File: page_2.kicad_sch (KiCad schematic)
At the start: 41 parts, among them J3 Conn_01x05, J601 USB_C_Receptacle_USB2.0_16P, SW1 SW_Push, SW2 SW_Push, T201 TP 201, U3 TCA9535PWR, U4 TCA9535PWR, U601 USBLC6-2SC6, U602 USBLC6-2SC6

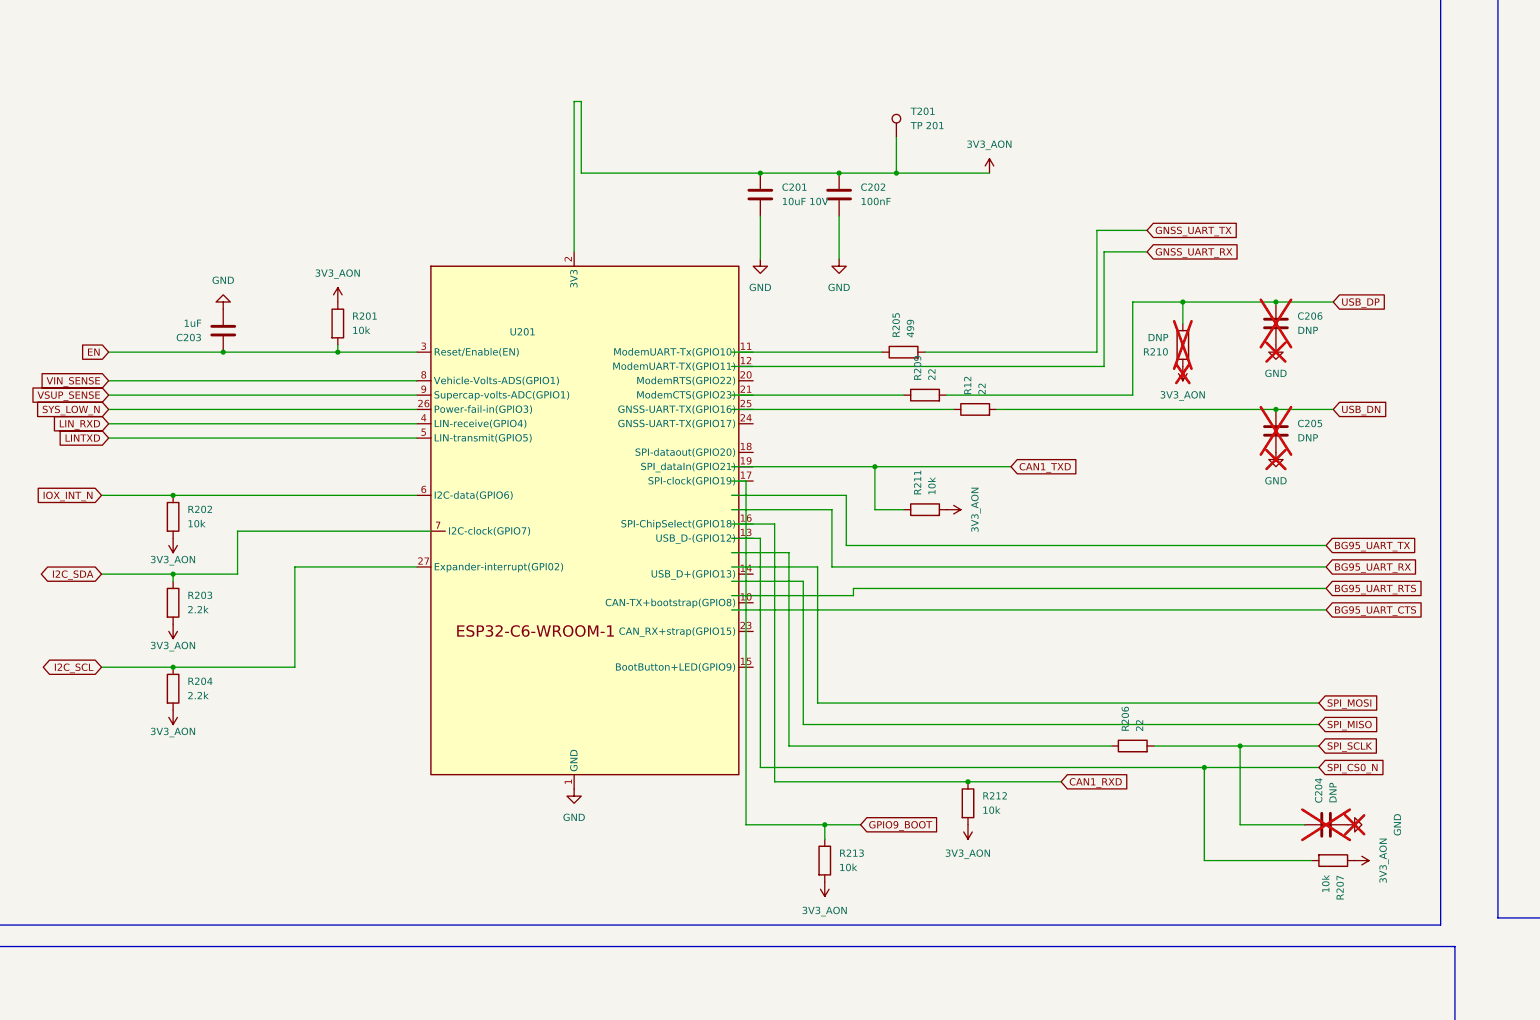
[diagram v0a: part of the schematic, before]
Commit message: Rework ESP32-C6 schematic routing
Updated the ESP32-C6-WROOM-1 schematic placement, pin naming, and net routing to match the intended board connectivity. This includes repositioning junctions/wires, correcting signal names like VehicleVolts-ADS and SupercapVolts-ADC, and aligning global labels/power symbols with the revised layout.
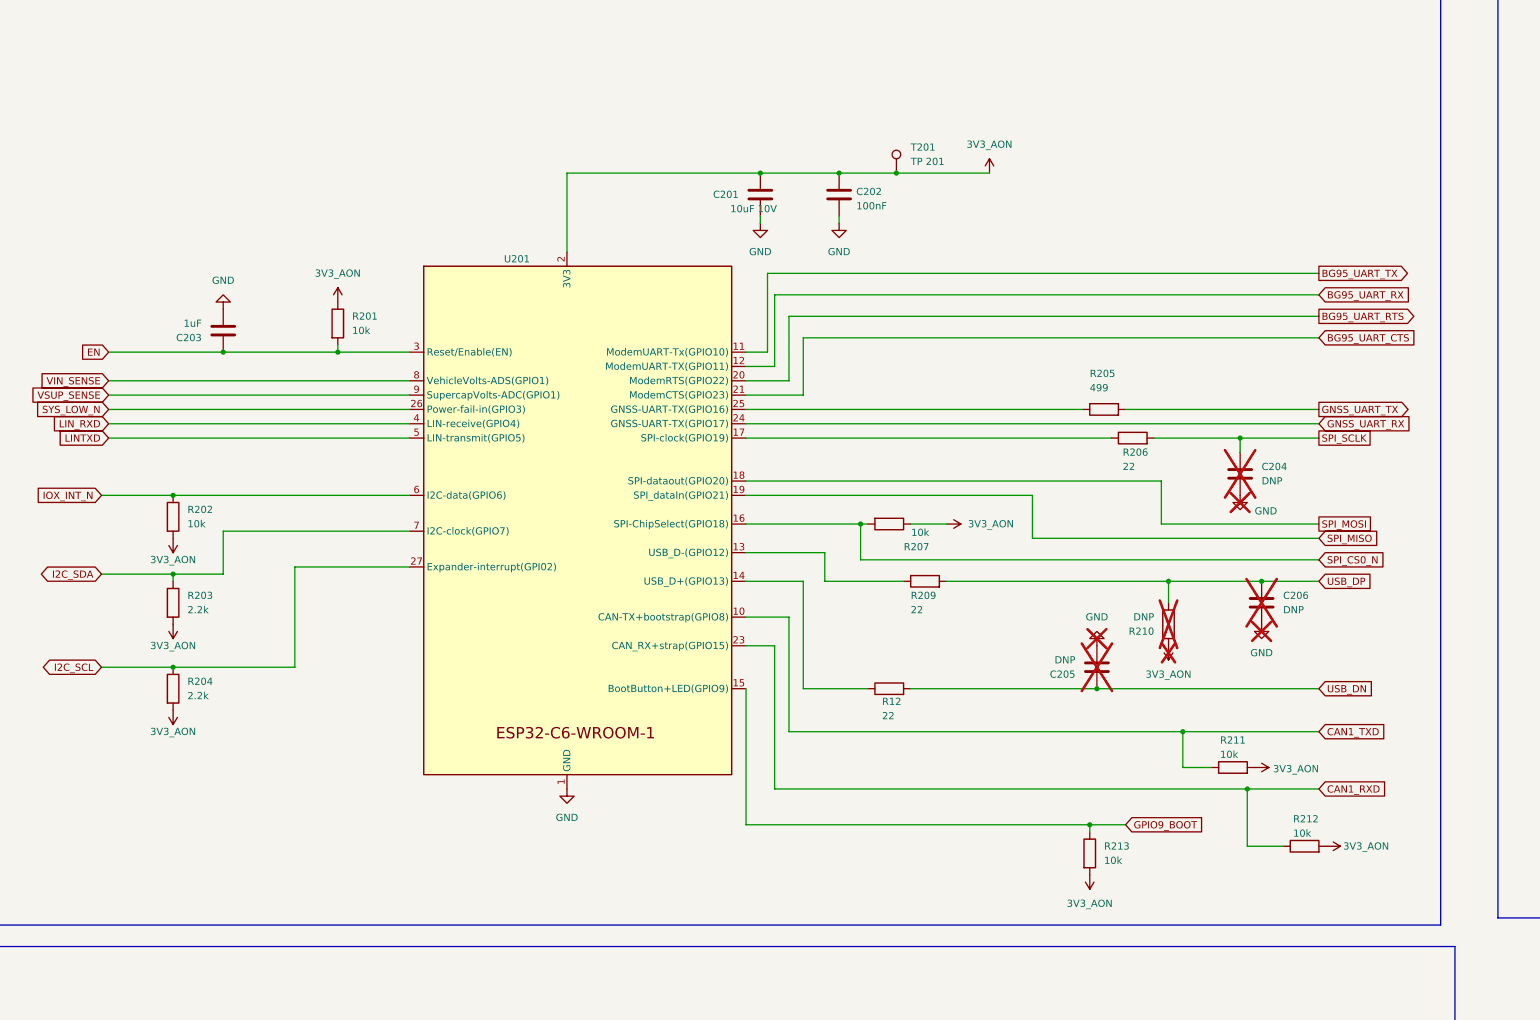
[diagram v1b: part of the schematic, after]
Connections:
- net BG95_UART_CTS: now also U201.21 (ModemCTS(GPIO23))
- net BG95_UART_RTS: now also U201.20 (ModemRTS(GPIO22))
- net BG95_UART_RX: now also U201.12 (ModemUART-TX(GPIO11))
- net BG95_UART_TX: now also U201.11 (ModemUART-Tx(GPIO10))
- net CAN1_RXD: now also U201.23 (CAN_RX+strap(GPIO15))
- net CAN1_TXD: now also U201.10 (CAN-TX+bootstrap(GPIO8))
- net GNSS_UART_RX: now also U201.24 (GNSS-UART-TX(GPIO17))
- net GPIO9_BOOT: now also U201.15 (BootButton+LED(GPIO9))
- net SPI_CS0_N: now also U201.16 (SPI-ChipSelect(GPIO18))
- net SPI_MISO: now also U201.19 (SPI_dataIn(GPIO21))
- net SPI_MOSI: now also U201.18 (SPI-dataout(GPIO20))
- net at R206.1: now also U201.17 (SPI-clock(GPIO19))
- net at R209.1: now also U201.13 (USB_D-(GPIO12))
- net at R12.1: now also U201.14 (USB_D+(GPIO13))
- net at R205.1: now also U201.25 (GNSS-UART-TX(GPIO16))
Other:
- moved on the sheet: C204, C205, C206, R12, R205, R206, R207, R209, R210, R211, R212, R213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

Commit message: Rework power/reset and USB protection
This schematic update adds a reset supervisor and associated support components, reworks the USB-C protection network and connector layout, and adds boot/reset/testpoint circuitry. It also reorganizes the ESP32-related blocks, updates labels and power nets, and moves the I/O-expander and peripheral sections to match the revised design.
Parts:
- removed C3: C, Package_SO:TSSOP-24_4.4x7.8mm_P0.65mm, symbol Device:C
- removed J3: Conn_01x05, symbol Connector_Generic:Conn_01x05
- removed R3: R, symbol Device:R
- removed R4: R, Package_TO_SOT_SMD:SOT-23-6, symbol Device:R
- removed SW1, SW2: SW_Push, Button_Switch_THT:SW_NKK_GW12LJP, symbol Switch:SW_Push
- removed TP3: TestPoint, symbol Connector:TestPoint
- added J201: Conn_01x05, symbol Connector_Generic:Conn_01x05
- added R214, R215: 1K, symbol Device:R
- added SW201: BOOT, Button_Switch_THT:SW_NKK_GW12LJP, symbol Switch:SW_Push
- added SW202: RESET, Button_Switch_THT:SW_NKK_GW12LJP, symbol Switch:SW_Push
- added TP202: TP 202, Relay_THT:Relay_DPDT_Schrack-RT2-FormC_RM5mm, symbol Connector:TestPoint
- added U203: TPS3840DL42DBVR, SOT95P280X145-5N, symbol TPS3840DL42DBVR:TPS3840DL42DBVR
- D2: value LED -> LED green; footprint Package_TO_SOT_THT:TO-220-2_Vertical -> LED_SMD:LED_Cree-XHP50_3V_HighDensity
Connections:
- net GPIO9_BOOT is gone; now on an unnamed net: R213.1, U201.15 (BootButton+LED(GPIO9))
- net IOX_IN_N is gone; now on an unnamed net: U3.1 (~{INT})
- net 3V3_AON: now also J201.1 (Pin_1), R214.1, U203.2 (VDD), U203.4 (~{MR}/NC)
- net GND: now also J201.5 (Pin_5), SW201.2, SW202.1, U203.3 (GND)
- net at D2.1 (K): now also J201.3 (Pin_3), SW201.1, TP202.1
- net at D2.2 (A): now also R214.2
- net EN: no longer names the net of C203.1, R201.2, U201.3 (Reset/Enable(EN))
- net EN: now also J201.2 (Pin_2), R215.2, SW202.2
- net GNSS_UART_TX: no longer names the net of R205.2
- net GNSS_UART_TX: now also J201.4 (Pin_4)
- net I2C_SCL: no longer names the net of R204.1, U201.27 (Expander-interrupt(GPI02)), U3.23 (SDA)
- net I2C_SDA: no longer names the net of R203.1, U201.7 (I2C-clock(GPIO7)), U3.22 (SCL)
- net IOX_INT_N: no longer names the net of R202.1, U201.6 (I2C-data(GPIO6))
- new net: R215.1, U203.1 (~{RESET})
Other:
- note added: "BOOT"
- note added: "DEBUG HEADER"
- note added: "ESP32-C6-WROOM-1U"
- note added: "I/O EXPANDER"
- moved on the sheet: C201, C202, C203, C204, C205, C206, C207, C601, D1, F106, J601, R12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

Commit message: Update page_2.kicad_sch
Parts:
- removed U4: TCA9535PWR, Package_SO:TSSOP-24_4.4x7.8mm_P0.65mm, symbol Interface_Expansion:TCA9535PWR
- added C208, C209, C210, C904, C908: 100nF, RF_Module:ESP32-C6-MINI-1, symbol Device:C
- added C702: 100nF, symbol Device:C
- added C901: 1uF, RF_Module:ESP32-C6-MINI-1, symbol Device:C
- added C902: 1nF, RF_Module:ESP32-C6-MINI-1, symbol Device:C
- added C907: 10uF 10V, RF_Module:ESP32-C6-MINI-1, symbol Device:C
- added J2: Micro_SD_Card_Det_Hirose_DM3AT, SOP65P640X120-16N, symbol Connector:Micro_SD_Card_Det_Hirose_DM3AT
- added R901: 100k, symbol Device:R
- added R903: 33, symbol Device:R
- added TP901: TP 901, SOT95P280X145-6N, symbol Connector:TestPoint
- added U401: W25N01GVZEIG_TR, SON127P800X600X80-9N-D, symbol W25N01GVZEIG_TR:W25N01GVZEIG_TR
- added U702: ATECC608B-SSHDA, Package_SO:SOIC-8_3.9x4.9mm_P1.27mm, symbol Security:ATECC608B-SSHDA
- added U901: TPS22918TDBVTQ1, SOT95P280X145-6N, symbol SamacSys_Parts:TPS22918TDBVTQ1
- added U902 (x2): SN74AXC4T245QPWRQ1, SOP65P640X120-16N, symbol SN74AXC4T245QPWRQ1:SN74AXC4T245QPWRQ1
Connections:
- net 3V3_AON: now also C208.1, C209.2, C210.2, C702.1, U702.8 (VCC), U902.1 (VCCA), U902.1 (VCCA), U902.16 (VCCB)
- net GND: now also C208.2, C209.1, C210.1, C702.2, C901.2, C902.2, C904.1, C907.2, C908.2, R901.2, U702.4 (GND), U901.5 (QOD), U902.14 (2~{OE}), U902.14 (2~{OE}), U902.15 (1~{OE}), U902.2 (1DIR), U902.2 (1DIR), U902.3 (2DIR), U902.3 (2DIR), U902.8 (GND_1), U902.9 (GND_2)
- net at R202.1, U201.6 (I2C-data(GPIO6)), U3.1 (~{INT}): now also U702.5 (SDA)
- net at R203.1, U201.7 (I2C-clock(GPIO7)), U3.22 (SCL): now also U702.6 (SCL)
- new net: J2.2 (DAT3/CD), U902.11 (2B1)
- new net: J2.3 (CMD), U902.12 (1B2)
- new net: C904.2, C907.1, C908.1, J2.4 (VDD), TP901.1, U901.1 (VIN), U901.2 (GND), U902.16 (VCCB)
- new net: J2.5 (CLK), R903.1
- new net: J2.7 (DAT0), U902.13 (1B1)
- new net: R901.1, U901.3 (ON)
- new net: C902.1, U901.4 (CT)
- new net: R903.2, U902.13 (1B1)
- new net 3V3_AUX: C901.1, U901.6 (VOUT)
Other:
- note added: "SD_PWR_EN"
- note added: "SECURE ELEMENT CHIP"

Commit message: Refine USB and power schematic layout
Updated component references and pin visibility in the KiCad sheet, including U901/U902/U903 renumbering, hidden passive pins, and adjusted ESP32/USB-C block placement. This also moves the SD card, power-switch, and signal labels to match the revised schematic layout and removes obsolete net labels.
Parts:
- renumbered U902 to U903
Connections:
- net CAN1_STBY is gone; now on an unnamed net: U3.19 (P16)
- net LIN_SLP_N is gone; now on an unnamed net: U3.20 (P17)
- net GND: now also U903.8 (GND_1), U903.9 (GND_2)
- net SPI_CS0_N: now also U401.1 (~{CS})
- net SPI_MISO: now also U401.2 (DO_(IO1))
- net at U401.5 (DI_(IO0)): now also U902.5 (1A2), U903.4 (1A1), U903.6 (2A1)
- net at U401.6 (CLK): now also U902.4 (1A1)
- net at U903.15 (1~{OE}): now also U902.6 (2A1)
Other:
- note removed: "SD_PWR_EN"
- moved on the sheet: C201, C202, C203, C204, C205, C206, C207, C208, C209, C210, C601, C702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

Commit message: Update page_2.kicad_sch
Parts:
- removed U401: W25N01GVZEIG_TR, SON127P800X600X80-9N-D, symbol W25N01GVZEIG_TR:W25N01GVZEIG_TR
- added C211, C212, C213, C214: 100nF, RF_Module:ESP32-C6-MINI-1, symbol Device:C
- added C401: 100uF, RF_Module:ESP32-C6-MINI-1, symbol Device:C
- added C402: 1nF, RF_Module:ESP32-C6-MINI-1, symbol Device:C
- added R401, R402, R801: 10k, symbol Device:R
- added R904, R905: 47K, symbol Device:R
- added TP401: TP 401, symbol Connector:TestPoint
- added TP402: TP 402, symbol Connector:TestPoint
- added TP403: TP 403, symbol Connector:TestPoint
- added TP404: TP 404, symbol Connector:TestPoint
- added U401: W25N01GVZEIG, SON127P800X600X80-9N-D, symbol SamacSys_Parts:W25N01GVZEIG
- added U801: ASM330LHHTR, LSM6DS3USTR, symbol SamacSys_Parts:ASM330LHHTR
- added U802: TMP1075DGKR, DGK0008A_N, symbol 2026-10-02_18-26-52:TMP1075DGKR
- TP901: footprint SOT95P280X145-6N -> (none)
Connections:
- net 3V3_AON: now also C211.1, C212.1, C213.1, C214.1, C401.2, C402.2, R401.2, R402.2, R801.2, U401.8 (VCC), U801.12 (CS), U801.5 (VDDIO), U801.8 (VDD), U802.8 (V+)
- net GND: now also J2.10 (DET_A), J2.6 (VSS), J2.SH (SHIELD), C211.2, C212.2, C213.2, C214.2, C401.1, C402.1, U401.4 (GND), U401.9 (EP), U801.1 (SDO/SA0), U801.2 (RES_1), U801.3 (RES_2), U801.6 (GND_1), U801.7 (GND_2), U802.4 (GND), U802.5 (A2), U802.6 (A1), U802.7 (A0)
- net IMU_INT1: now also U801.4 (INT1)
- net USB_DN: now also J601.A7 (D-), J601.B7 (D-), U601.1 (I/O1), U601.6 (I/O1)
- net USB_DP: now also J601.A6 (D+), J601.B6 (D+), U601.3 (I/O2), U601.4 (I/O2)
- net at J2.3 (CMD), U902.12 (1B2): now also R904.1
- net at J2.7 (DAT0), U903.13 (1B1): now also R905.1
- net CC1: now reaches J601.A5 (CC1), R601.1
- net CC1: now also U602.1 (I/O1), U602.6 (I/O1)
- net CC2: now reaches J601.B5 (CC2), R602.1
- net CC2: now also U602.3 (I/O2), U602.4 (I/O2)
- net at U902.5 (1A2), U903.4 (1A1): now also TP403.1, U401.5 (DI_(IO0_)); no longer U903.6 (2A1)
- net at U902.4 (1A1): now also TP402.1, U401.6 (CLK)
- net at R202.1, U201.6 (I2C-data(GPIO6)), U3.1 (~{INT})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: now also U801.14 (SDA), U802.1 (SDA)
- net at R203.1, U201.7 (I2C-clock(GPIO7)), U3.22 (SCL)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: now also U801.13 (SCL), U802.2 (SCL)
- net SPI_CS0_N: no longer names the net of R207.2, U201.16 (SPI-ChipSelect(GPIO18))
- net SPI_CS0_N: now also TP401.1, U401.1 (~{CS})
- net SPI_MISO: no longer names the net of U201.19 (SPI_dataIn(GPIO21))
- net SPI_MISO: now also TP404.1, U401.2 (DO_(IO1_))
- new net: R801.1, U802.3 (ALERT)
- new net: R401.1, U401.3 (~{WP_(IO2_)})
- new net: R402.1, U401.7 (~{HOLD_(IO3_)})
- new net SD_VDD: R904.2, R905.2
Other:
- note added: "I2C_SCL"
- note added: "I2C_SDA"
- note added: "IMU_INT2"
- note added: "MICRO-SD CARD"
- note added: "MOTION SENSOR"
- note added: "RESET"
- note added: "SPI_CS0_N"
- note added: "SPI_MISO"
- note added: "TELEMETRY STORAGE"
- note added: "TEMP SENSOR"
- note added: "TEMP_ALERT_N"
- note removed: "CC1"
- note removed: "CC2"
- note removed: "USB_DN"
- note removed: "USB_DP"
- moved on the sheet: C201, C202, C203, C204, C205, C206, C207, C208, C209, C210, C601, C702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

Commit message: Add project library symbols and KiCad updates
This change updates the KiCad project to use the Project_Parts symbol library and refreshes the tracker schematic symbol metadata. It adds the SN74AXC4T245 level shifter, BG95 modem and SIM connector references, and associated decoupling/ground net connections. The patch also restores the ESP32-C6 and ASM330 symbols to the current design and registers the new project symbol library in sym-lib-table.
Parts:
- U201: symbol PCM_Espressif:ESP32-C6-WROOM-1 -> Project_Parts:ESP32-C6-WROOM-1
- U203: footprint SOT95P280X145-5N -> SamacSys_Parts:SOT95P280X145-6N
- U801: footprint LSM6DS3USTR -> SamacSys_Parts:LSM6DS3USTR; symbol SamacSys_Parts:ASM330LHHTR -> Project_Parts:ASM330LHHTR
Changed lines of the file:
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@@
 			)
 		)
-		(property "Footprint" "SOT95P280X145-5N"
+		(property "Footprint" "SamacSys_Parts:SOT95P280X145-6N"
 			(at 80.01 182.55 0)
 			(hide yes)
@@
 	)
 	(symbol
-		(lib_id "PCM_Espressif:ESP32-C6-WROOM-1")
+		(lib_id "Project_Parts:ESP32-C6-WROOM-1")
 		(at 261.62 115.57 0)
 		(unit 1)
@@
 	)
 	(symbol
-		(lib_id "SamacSys_Parts:ASM330LHHTR")
+		(lib_id "Project_Parts:ASM330LHHTR")
 		(at 173.99 342.9 0)
 		(unit 1)
@@
 			)
 		)
-		(property "Footprint" "LSM6DS3USTR"
+		(property "Footprint" "SamacSys_Parts:LSM6DS3USTR"
 			(at 205.74 430.2 0)
 			(hide yes)
